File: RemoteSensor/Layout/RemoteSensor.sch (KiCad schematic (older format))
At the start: 20 parts, among them Q1 2N7002, U1 ESP-12F, U2 74LVC2G02

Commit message: Add lipo support
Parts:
- removed S?: JOYSTICK_MINI, JOYSTICK_MINI, symbol SparkFun-Switches:JOYSTICK_MINI
- added C?: 4.7u, symbol Device:C
- added C?: 10u, symbol Device:C
- added C? (x2): 1u, symbol Device:C
- added C? (x2): 0.1u, symbol Device:C
- added J?: USB_B_Micro, Connector_USB:USB_Micro-B_Molex-105133-0031, symbol Connector:USB_B_Micro
- added L?: 2.2u, symbol Device:L
- added Q?: 2N7002, digikey-footprints:SOT-23-3, symbol dk_Transistors-FETs-MOSFETs-Single:2N7002
- added R10, R11: 1k, Resistor_SMD:R_0603_1608Metric_Pad1.05x0.95mm_HandSolder, symbol Device:R_US
- added R? (x3): 10k, symbol Device:R_US
- added R?: 2k, symbol Device:R_US
- added S1: NAV_SWITCH, NAV_SWITCH, symbol SparkFun-Switches:NAV_SWITCH
- added U?: LM3670MF, Package_TO_SOT_SMD:TSOT-23-5, symbol Regulator_Switching:LM3670MF
- added U? (x2): BD48ExxG, Package_TO_SOT_SMD:SOT-23-5, symbol Power_Management:BD48ExxG
- added U?: MCP73831-2-OT, Package_TO_SOT_SMD:SOT-23-5, symbol Battery_Management:MCP73831-2-OT
- J1: renamed from J?; footprint (none) -> Connector_PinSocket_2.54mm:PinSocket_1x03_P2.54mm_Vertical
- R5, R6: renamed from R?; value R_US -> 4.7k; footprint (none) -> Resistor_SMD:R_0603_1608Metric_Pad1.05x0.95mm_HandSolder
- R8, R9: renamed from R?; footprint (none) -> Resistor_SMD:R_0603_1608Metric_Pad1.05x0.95mm_HandSolder
- SW1, SW2: renamed from SW?; footprint (none) -> Button_Switch_SMD:SW_SPST_TL3342
- gave numbers to parts that had none: 5
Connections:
- net labels added: BATT_STS, CENTER_PIN, CHARGER_STS, DOWN_PIN, SLEEP_STS, UP_PIN, V_BATT, V_USB, WAKE_STS
- net labels removed: BTN_CENTER, BTN_DOWN, BTN_LEFT, BTN_RIGHT, BTN_UP, UP_BTN
- wire segments 80 -> 142
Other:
- moved on the sheet: Q1, R2, R3, R4, U2A, U2B

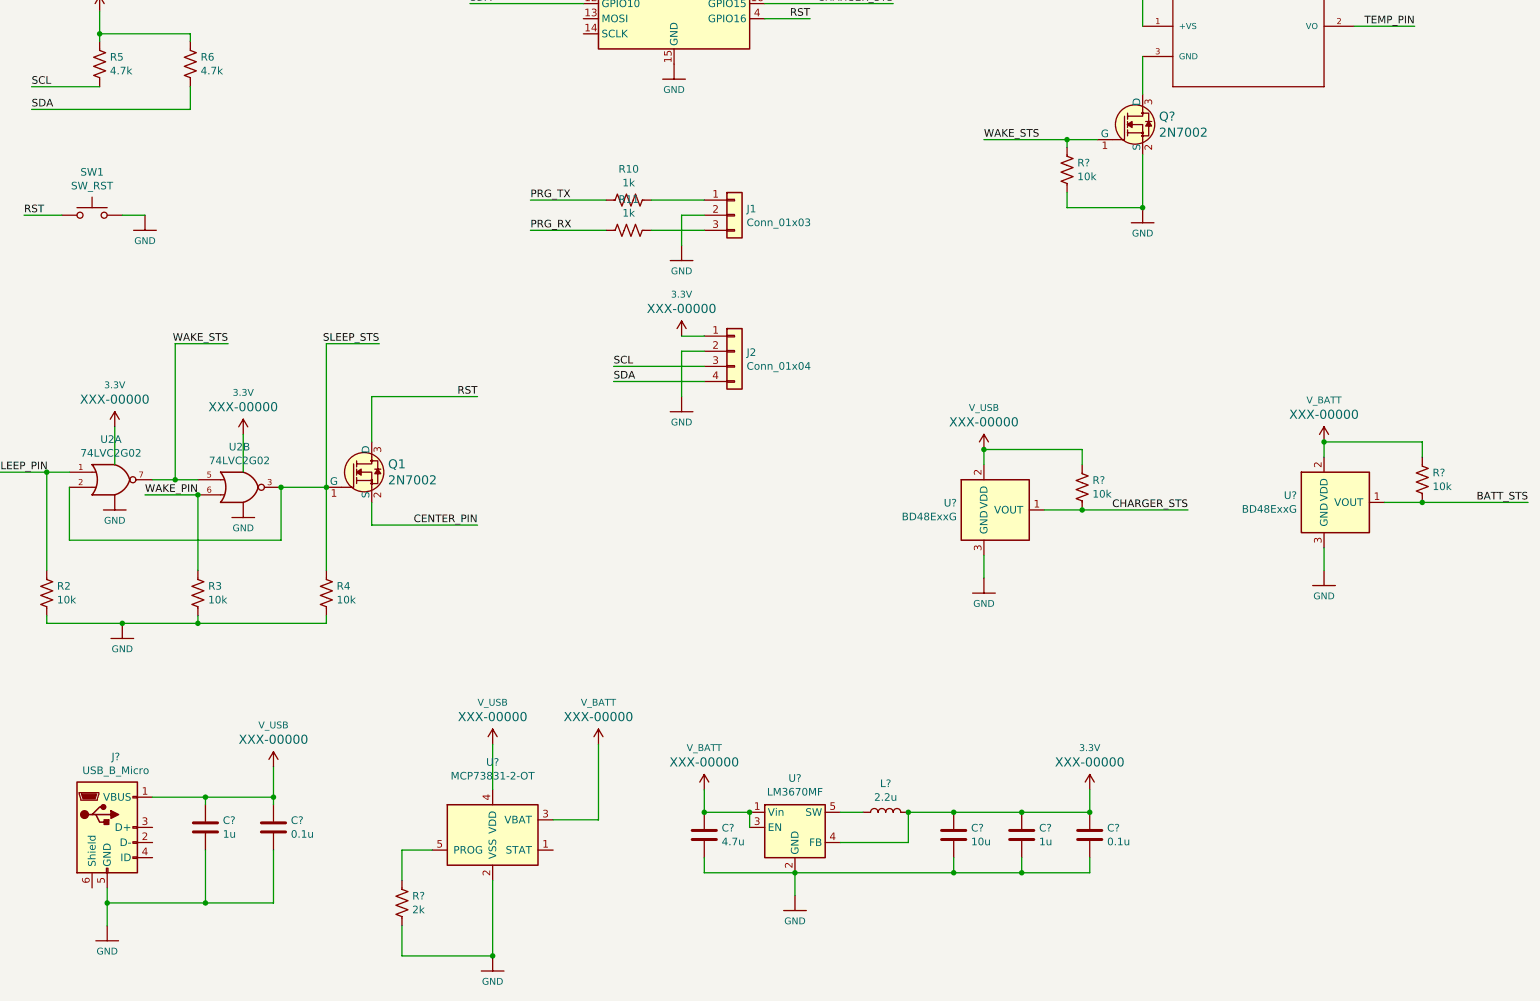
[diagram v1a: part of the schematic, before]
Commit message: Finish schematic
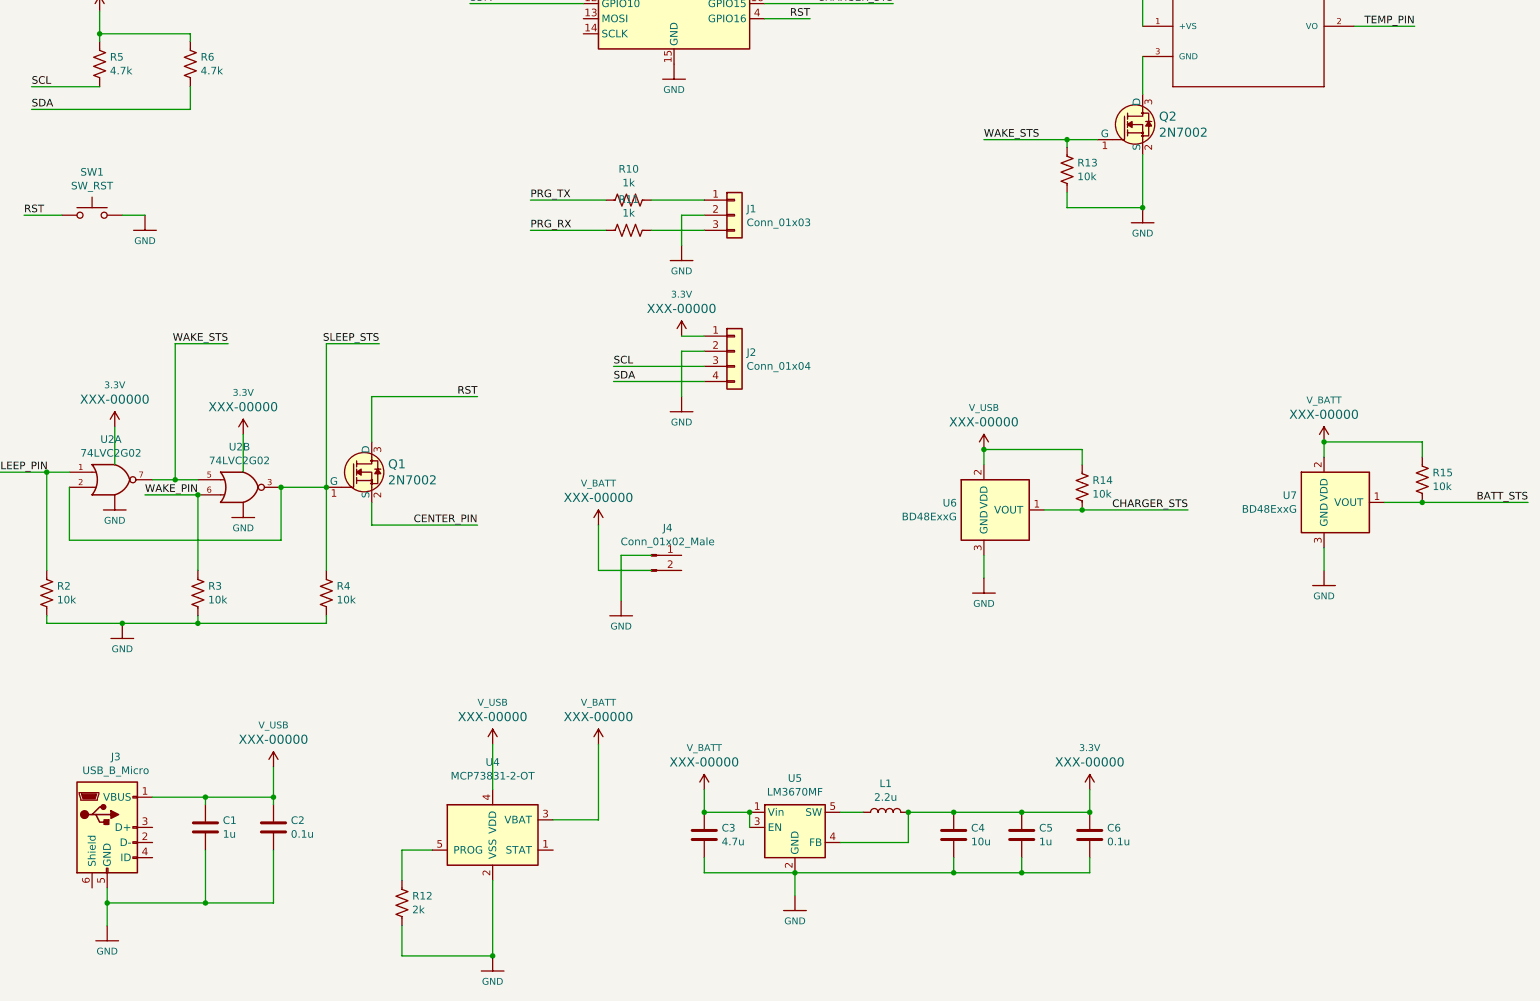
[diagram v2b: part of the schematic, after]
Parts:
- added J4: Conn_01x02_Male, Connector_JST:JST_PH_S2B-PH-SM4-TB_1x02-1MP_P2.00mm_Horizontal, symbol Connector:Conn_01x02_Male
- C1, C2, C3, C4, C5, C6: renamed from C?; footprint (none) -> Capacitor_SMD:C_0603_1608Metric_Pad1.05x0.95mm_HandSolder
- D1, D2: footprint (none) -> LED_SMD:LED_0603_1608Metric_Pad1.05x0.95mm_HandSolder
- J2: footprint (none) -> Connector_PinHeader_2.54mm:PinHeader_1x04_P2.54mm_Vertical
- L1: renamed from L?; footprint (none) -> Inductor_SMD:L_0603_1608Metric_Pad1.05x0.95mm_HandSolder
- R12, R13, R14, R15: renamed from R?; footprint (none) -> Resistor_SMD:R_0603_1608Metric_Pad1.05x0.95mm_HandSolder
- gave numbers to parts that had none: 6

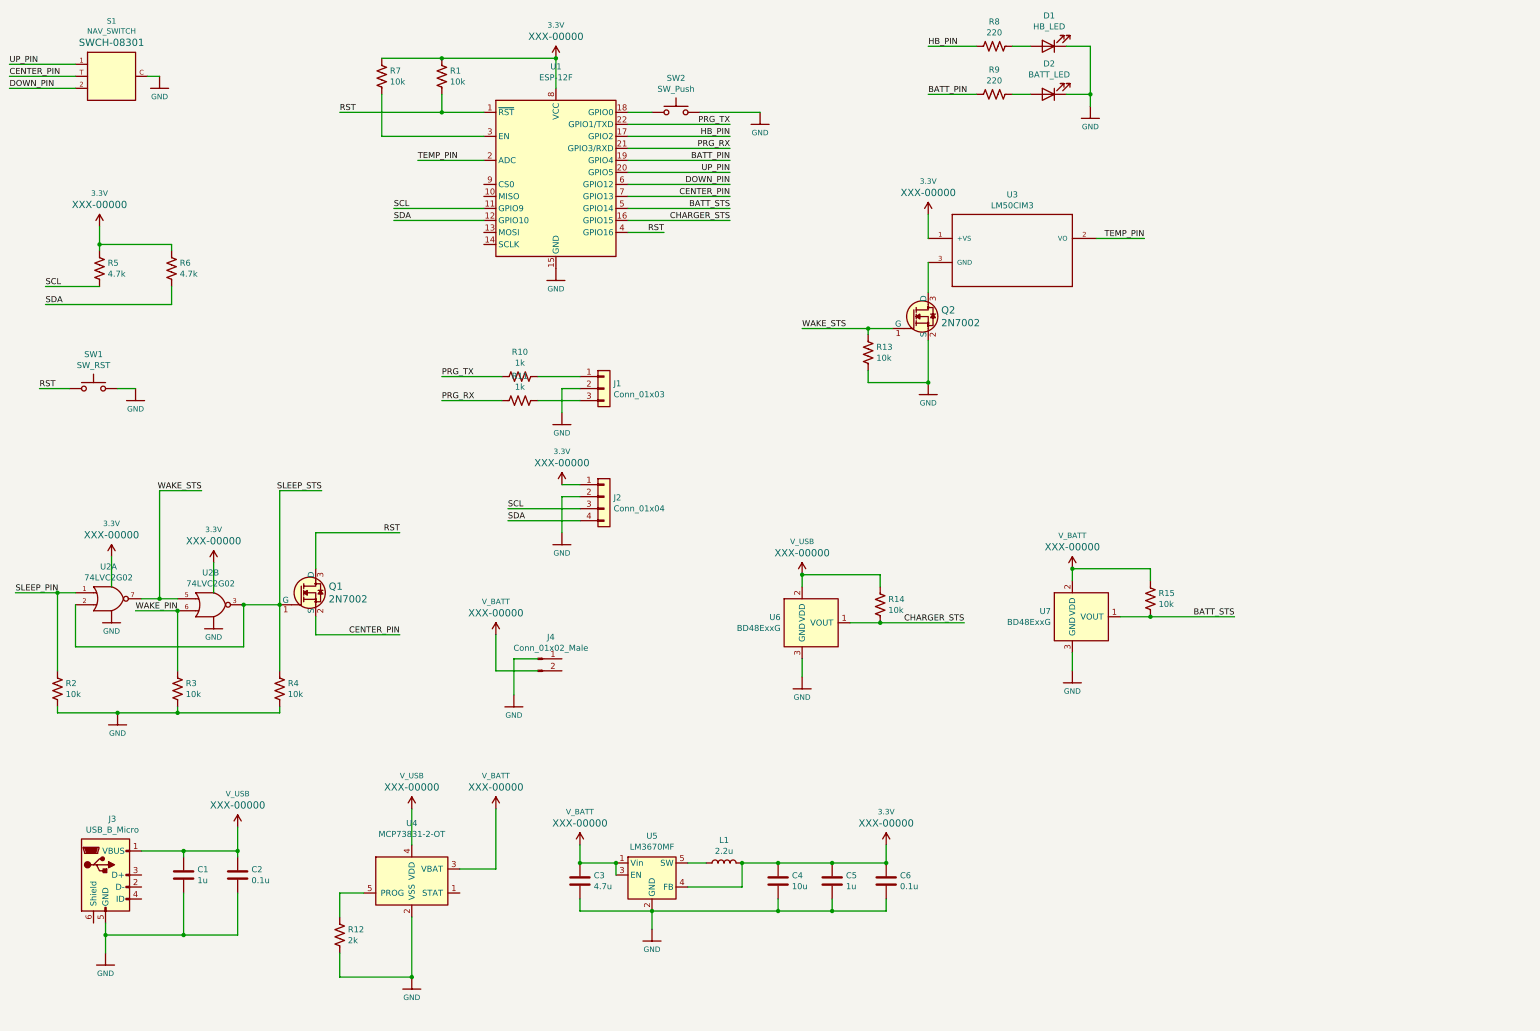
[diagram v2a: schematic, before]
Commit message: More power control. Add some mounting holes.
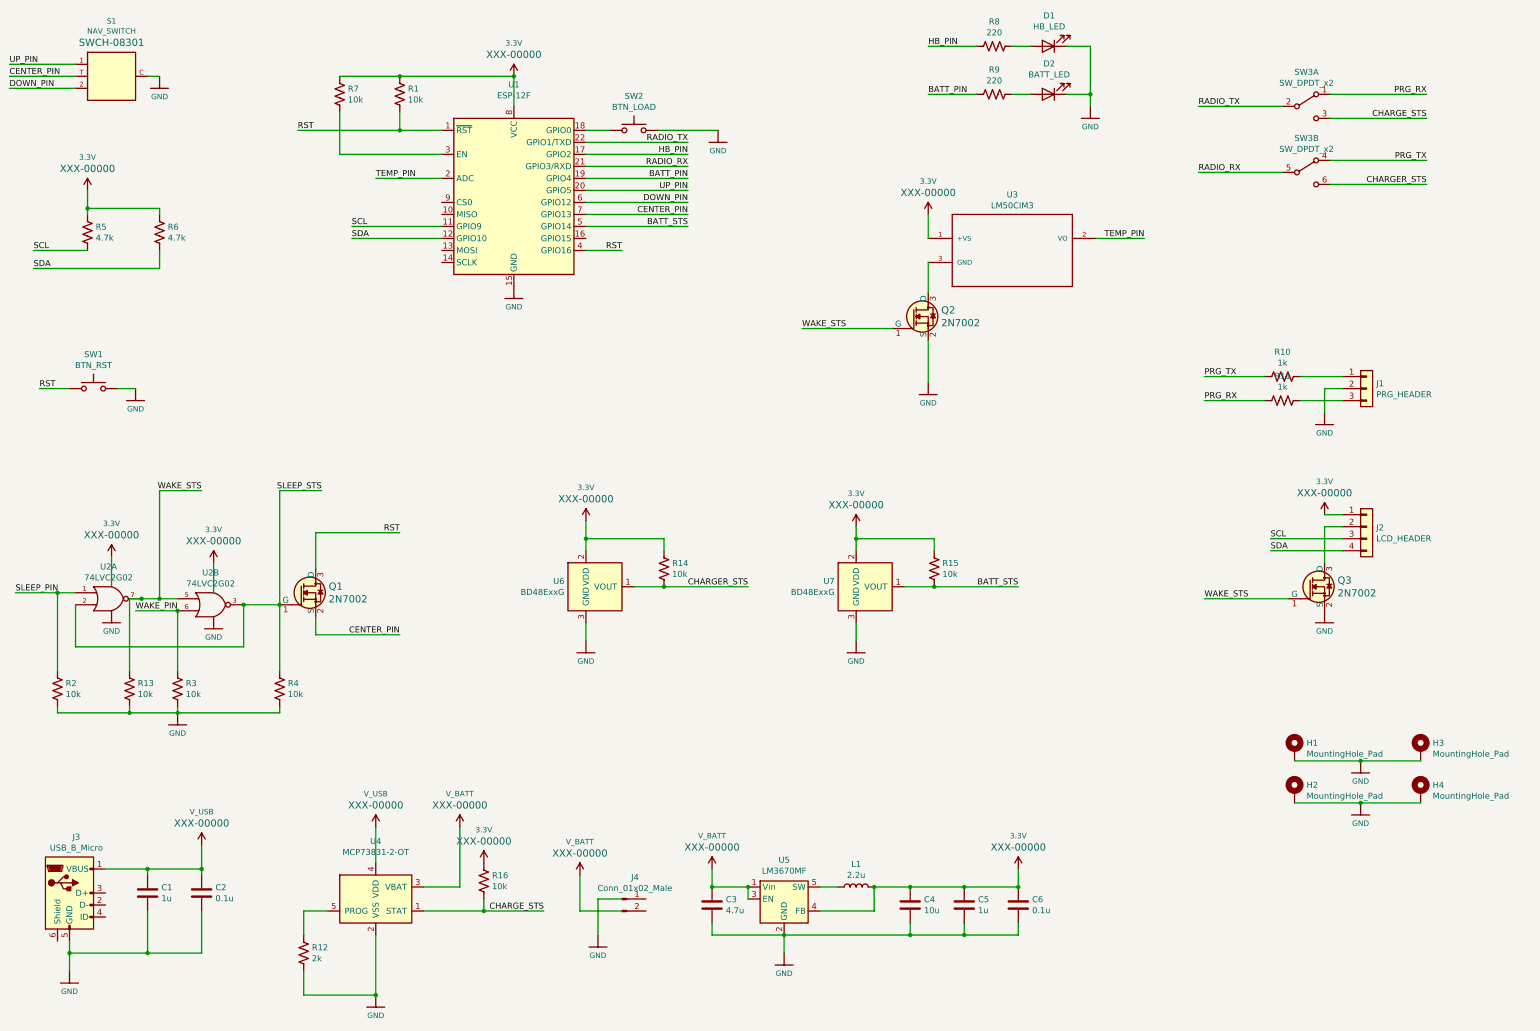
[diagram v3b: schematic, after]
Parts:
- added H1, H2, H3, H4: MountingHole_Pad, MountingHole:MountingHole_2.7mm_M2.5_DIN965_Pad, symbol Mechanical:MountingHole_Pad
- added Q3: 2N7002, digikey-footprints:SOT-23-3, symbol dk_Transistors-FETs-MOSFETs-Single:2N7002
- added R16: 10k, Resistor_SMD:R_0603_1608Metric_Pad1.05x0.95mm_HandSolder, symbol Device:R_US
- added SW3: SW_DPDT_x2, Switches:SWITCH_DPDT_SMD_AYZ0202, symbol Switch:SW_DPDT_x2
- J1: value Conn_01x03 -> PRG_HEADER
- J2: value Conn_01x04 -> LCD_HEADER
- SW1: value SW_RST -> BTN_RST
- SW2: value SW_Push -> BTN_LOAD
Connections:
- net 3.3V: now also R14.1, R15.1, U6.2 (VDD), U7.2 (VDD), R16.1
- net CHARGER_STS: now also SW3.6 (C); no longer U1.16 (GPIO15)
- net GND: now also H1.1, H2.1, H3.1, H4.1, Q3.2 (S); no longer J2.2 (Pin_2)
- net PRG_RX: now also SW3.1 (A); no longer U1.21 (GPIO3/RXD)
- net PRG_TX: now also SW3.4 (A); no longer U1.22 (GPIO1/TXD)
- net V_BATT: no longer R15.1, U7.2 (VDD)
- net V_USB: no longer R14.1, U6.2 (VDD)
- net WAKE_STS: now also Q3.1 (G)
- net CHARGE_STS: now reaches U4.1 (STAT)
- net CHARGE_STS: now also R16.2, SW3.3 (C)
- new net: J2.2 (Pin_2), Q3.3 (D)
- new net RADIO_RX: SW3.5 (B), U1.21 (GPIO3/RXD)
- new net RADIO_TX: SW3.2 (B), U1.22 (GPIO1/TXD)
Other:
- moved on the sheet: C1, C2, C3, C4, C5, C6, J1, J2, J3, J4, L1, R1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

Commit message: Finalize PCB
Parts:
- J3: footprint Connector_USB:USB_Micro-B_Molex-105133-0031 -> Connector_USB:USB_Micro-B_Molex_47346-0001
- J4: value Conn_01x02_Male -> BATT_CONN
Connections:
- net WAKE_PIN is gone; now on net HB_PIN: R3.1, U2.6
- net GND: now also J3.6 (Shield), J4.1 (Pin_1)
- net SLEEP_PIN: now also U1.16 (GPIO15)
- net V_BATT: now also J4.2 (Pin_2)
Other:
- moved on the sheet: J4
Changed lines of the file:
@@
 SLEEP_PIN
 Text Label 1900 5800 0    50   ~ 0
-WAKE_PIN
+HB_PIN
 $Comp
 L Device:LED D1
@@
 F 0 "J3" H 1407 8617 50  0000 C CNN
 F 1 "USB_B_Micro" H 1407 8526 50  0000 C CNN
-F 2 "Connector_USB:USB_Micro-B_Molex-105133-0031" H 1500 8100 50  0001 C CNN
+F 2 "Connector_USB:USB_Micro-B_Molex_47346-0001" H 1500 8100 50  0001 C CNN
 F 3 "~" H 1500 8100 50  0001 C CNN
 	1    1350 8150
@@
 L Connector:Conn_01x02_Male J4
 U 1 1 5ED30E4E
-P 5950 8200
-F 0 "J4" H 6058 8381 50  0000 C CNN
-F 1 "Conn_01x02_Male" H 6058 8290 50  0000 C CNN
-F 2 "Connector_JST:JST_PH_S2B-PH-SM4-TB_1x02-1MP_P2.00mm_Horizontal" H 5950 8200 50  0001 C CNN
-F 3 "~" H 5950 8200 50  0001 C CNN
-	1    5950 8200
+P 5600 8200
+F 0 "J4" H 5708 8381 50  0000 C CNN
+F 1 "BATT_CONN" H 5708 8290 50  0000 C CNN
+F 2 "Connector_JST:JST_PH_S2B-PH-SM4-TB_1x02-1MP_P2.00mm_Horizontal" H 5600 8200 50  0001 C CNN
+F 3 "~" H 5600 8200 50  0001 C CNN
+	1    5600 8200
 	1    0    0    -1
 $EndComp
@@
 L SparkFun-PowerSymbols:GND #GND0117
 U 1 1 5ED32AFF
-P 5750 8500
-F 0 "#GND0117" H 5800 8450 45  0001 L BNN
-F 1 "GND" H 5750 8330 45  0000 C CNN
-F 2 "" H 5750 8400 60  0001 C CNN
-F 3 "" H 5750 8400 60  0001 C CNN
-	1    5750 8500
-	1    0    0    -1
-$EndComp
-Wire Wire Line
-	5950 8200 5750 8200
-Wire Wire Line
-	5750 8200 5750 8500
+P 6050 8450
+F 0 "#GND0117" H 6100 8400 45  0001 L BNN
+F 1 "GND" H 6050 8280 45  0000 C CNN
+F 2 "" H 6050 8350 60  0001 C CNN
+F 3 "" H 6050 8350 60  0001 C CNN
+	1    6050 8450
+	1    0    0    -1
+$EndComp
 $Comp
 L SparkFun-PowerSymbols:V_BATT #SUPPLY0114
 U 1 1 5ED399F5
-P 5600 8000
-F 0 "#SUPPLY0114" H 5650 8000 45  0001 L BNN
-F 1 "V_BATT" H 5600 8276 45  0000 C CNN
-F 2 "XXX-00000" H 5600 8181 60  0000 C CNN
-F 3 "" H 5600 8000 60  0001 C CNN
-	1    5600 8000
-	1    0    0    -1
-$EndComp
-Wire Wire Line
-	5950 8300 5600 8300
-Wire Wire Line
-	5600 8300 5600 8000
+P 6100 8000
+F 0 "#SUPPLY0114" H 6150 8000 45  0001 L BNN
+F 1 "V_BATT" H 6100 8276 45  0000 C CNN
+F 2 "XXX-00000" H 6100 8181 60  0000 C CNN
+F 3 "" H 6100 8000 60  0001 C CNN
+	1    6100 8000
+	1    0    0    -1
+$EndComp
 Wire Wire Line
 	7450 3450 8200 3450
@@
 Wire Wire Line
 	12100 7400 12600 7400
+Wire Wire Line
+	5650 2700 6500 2700
+Text Label 6500 2700 2    50   ~ 0
+SLEEP_PIN
+Wire Wire Line
+	1250 8550 1250 8650
+Wire Wire Line
+	1250 8650 1350 8650
+Wire Wire Line
+	5800 8300 6100 8300
+Wire Wire Line
+	6100 8300 6100 8000
+Wire Wire Line
+	5800 8200 6050 8200
+Wire Wire Line
+	6050 8200 6050 8450
 $EndSCHEMATC
